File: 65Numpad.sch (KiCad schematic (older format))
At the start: 137 parts

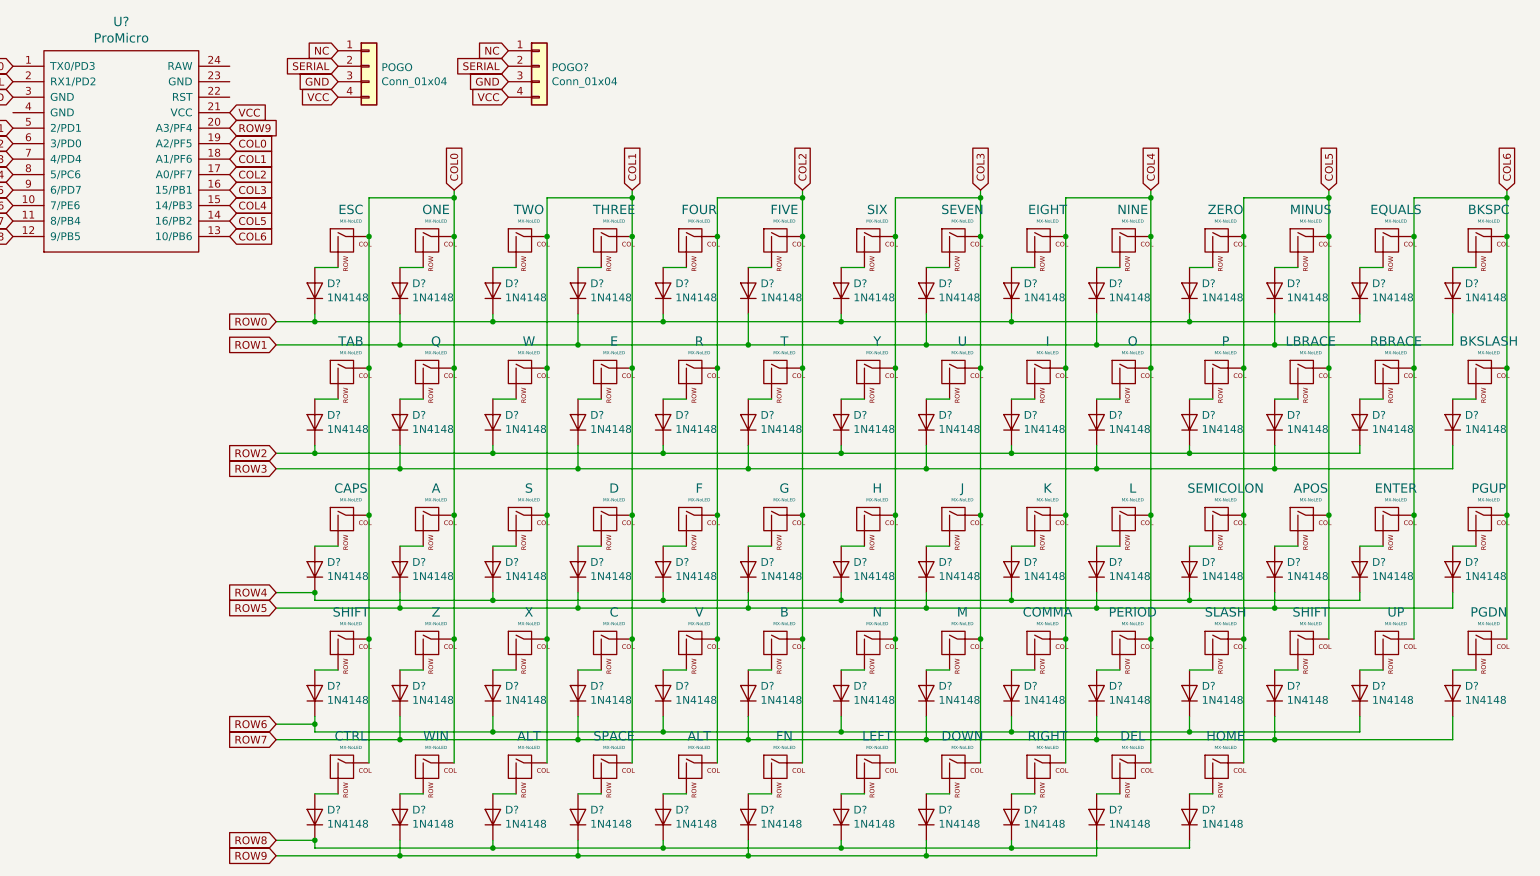
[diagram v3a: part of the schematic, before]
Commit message: Finished assigning footprints
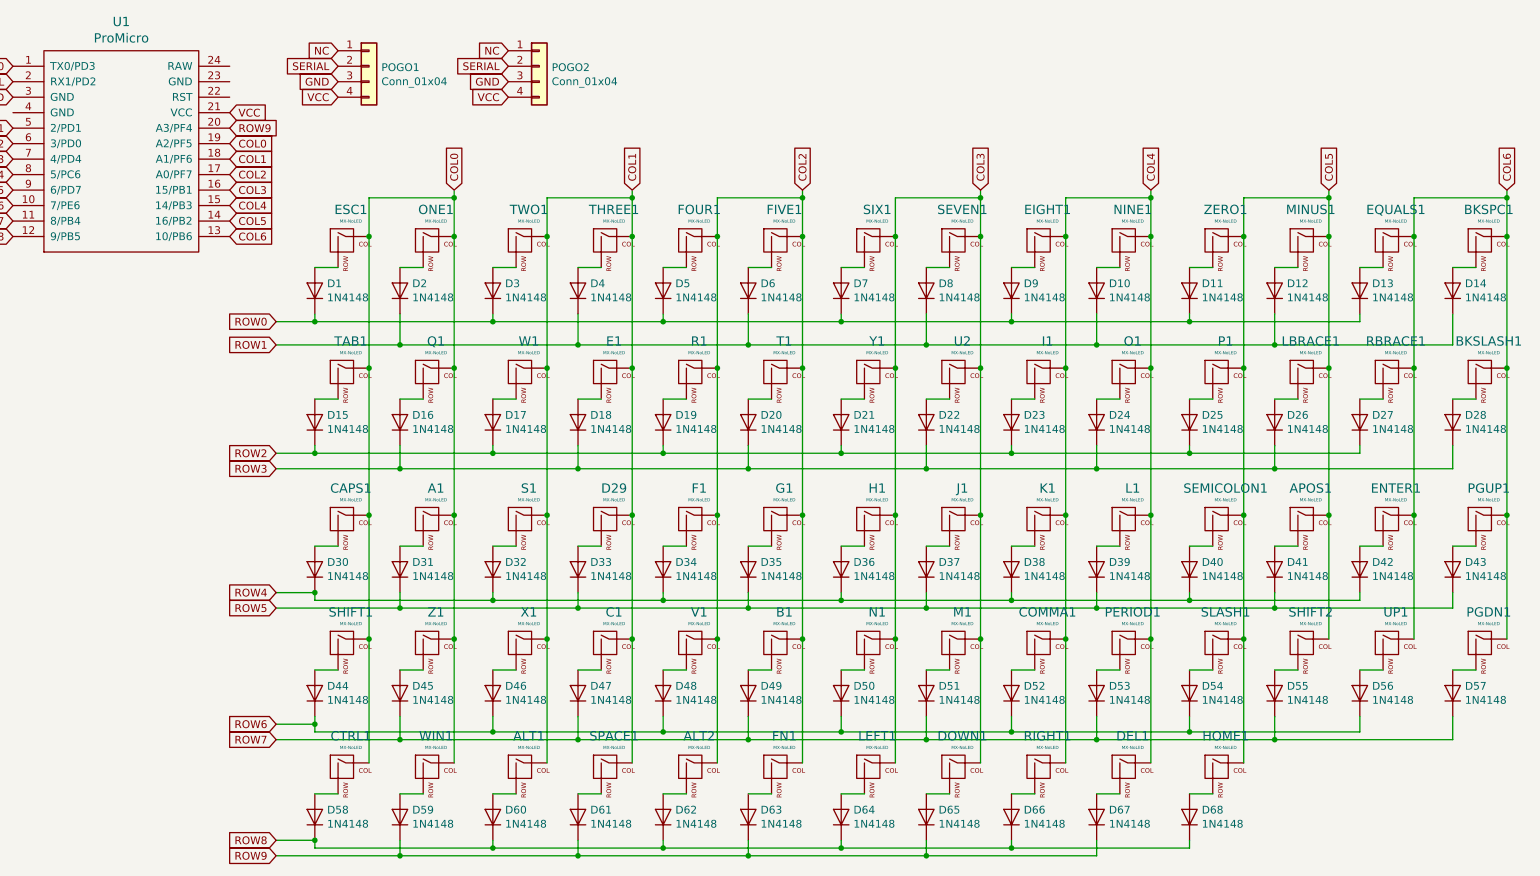
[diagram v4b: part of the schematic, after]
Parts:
- A1: renamed from A; footprint (none) -> MX_Only:MXOnly-1U-NoLED
- ALT1, ALT2: renamed from ALT; footprint (none) -> MX_Only:MXOnly-1.25U-NoLED
- APOS1: renamed from APOS; footprint (none) -> MX_Only:MXOnly-1U-NoLED
- B1: renamed from B; footprint (none) -> MX_Only:MXOnly-1U-NoLED
- BKSLASH1: renamed from BKSLASH; footprint (none) -> MX_Only:MXOnly-1.5U-NoLED
- BKSPC1: renamed from BKSPC; footprint (none) -> MX_Only:MXOnly-2U-NoLED
- C1: renamed from C; footprint (none) -> MX_Only:MXOnly-1U-NoLED
- CAPS1: renamed from CAPS; footprint (none) -> MX_Only:MXOnly-1.75U-NoLED
- COMMA1: renamed from COMMA; footprint (none) -> MX_Only:MXOnly-1U-NoLED
- CTRL1: renamed from CTRL; footprint (none) -> MX_Only:MXOnly-1.25U-NoLED
- D29: renamed from D; footprint (none) -> MX_Only:MXOnly-1U-NoLED
- DEL1: renamed from DEL; footprint (none) -> MX_Only:MXOnly-1U-NoLED
- DOWN1: renamed from DOWN; footprint (none) -> MX_Only:MXOnly-1U-NoLED
- E1: renamed from E; footprint (none) -> MX_Only:MXOnly-1U-NoLED
- EIGHT1: renamed from EIGHT; footprint (none) -> MX_Only:MXOnly-1U-NoLED
- ENTER1: renamed from ENTER; footprint (none) -> MX_Only:MXOnly-2.25U-NoLED
- EQUALS1: renamed from EQUALS; footprint (none) -> MX_Only:MXOnly-1U-NoLED
- ESC1: renamed from ESC; footprint (none) -> MX_Only:MXOnly-1U-NoLED
- F1: renamed from F; footprint (none) -> MX_Only:MXOnly-1U-NoLED
- FIVE1: renamed from FIVE; footprint (none) -> MX_Only:MXOnly-1U-NoLED
- FN1: renamed from FN; footprint (none) -> MX_Only:MXOnly-1.25U-NoLED
- FOUR1: renamed from FOUR; footprint (none) -> MX_Only:MXOnly-1U-NoLED
- G1: renamed from G; footprint (none) -> MX_Only:MXOnly-1U-NoLED
- H1: renamed from H; footprint (none) -> MX_Only:MXOnly-1U-NoLED
- HOME1: renamed from HOME; footprint (none) -> MX_Only:MXOnly-1U-NoLED
- I1: renamed from I; footprint (none) -> MX_Only:MXOnly-1U-NoLED
- J1: renamed from J; footprint (none) -> MX_Only:MXOnly-1U-NoLED
- K1: renamed from K; footprint (none) -> MX_Only:MXOnly-1U-NoLED
- L1: renamed from L; footprint (none) -> MX_Only:MXOnly-1U-NoLED
- LBRACE1: renamed from LBRACE; footprint (none) -> MX_Only:MXOnly-1U-NoLED
- LEFT1: renamed from LEFT; footprint (none) -> MX_Only:MXOnly-1U-NoLED
- M1: renamed from M; footprint (none) -> MX_Only:MXOnly-1U-NoLED
- MINUS1: renamed from MINUS; footprint (none) -> MX_Only:MXOnly-1U-NoLED
- N1: renamed from N; footprint (none) -> MX_Only:MXOnly-1U-NoLED
- NINE1: renamed from NINE; footprint (none) -> MX_Only:MXOnly-1U-NoLED
- O1: renamed from O; footprint (none) -> MX_Only:MXOnly-1U-NoLED
- ONE1: renamed from ONE; footprint (none) -> MX_Only:MXOnly-1U-NoLED
- P1: renamed from P; footprint (none) -> MX_Only:MXOnly-1U-NoLED
- PERIOD1: renamed from PERIOD; footprint (none) -> MX_Only:MXOnly-1U-NoLED
- PGDN1: renamed from PGDN; footprint (none) -> MX_Only:MXOnly-1U-NoLED
- PGUP1: renamed from PGUP; footprint (none) -> MX_Only:MXOnly-1U-NoLED
- POGO1: renamed from POGO; footprint (none) -> Pin_Headers:Pin_Header_Angled_1x04_Pitch2.54mm
- POGO2: renamed from POGO?; footprint (none) -> Pin_Headers:Pin_Header_Angled_1x04_Pitch2.54mm
- Q1: renamed from Q; footprint (none) -> MX_Only:MXOnly-1U-NoLED
- R1: renamed from R; footprint (none) -> MX_Only:MXOnly-1U-NoLED
- RBRACE1: renamed from RBRACE; footprint (none) -> MX_Only:MXOnly-1U-NoLED
- RIGHT1: renamed from RIGHT; footprint (none) -> MX_Only:MXOnly-1U-NoLED
- S1: renamed from S; footprint (none) -> MX_Only:MXOnly-1U-NoLED
- SEMICOLON1: renamed from SEMICOLON; footprint (none) -> MX_Only:MXOnly-1U-NoLED
- SEVEN1: renamed from SEVEN; footprint (none) -> MX_Only:MXOnly-1U-NoLED
- SHIFT1: renamed from SHIFT; footprint (none) -> MX_Only:MXOnly-2.25U-NoLED
- SHIFT2: renamed from SHIFT; footprint (none) -> MX_Only:MXOnly-1.75U-NoLED
- SIX1: renamed from SIX; footprint (none) -> MX_Only:MXOnly-1U-NoLED
- SLASH1: renamed from SLASH; footprint (none) -> MX_Only:MXOnly-1U-NoLED
- SPACE1: renamed from SPACE; footprint (none) -> MX_Only:MXOnly-6.25U-NoLED
- T1: renamed from T; footprint (none) -> MX_Only:MXOnly-1U-NoLED
- TAB1: renamed from TAB; footprint (none) -> MX_Only:MXOnly-1.5U-NoLED
- THREE1: renamed from THREE; footprint (none) -> MX_Only:MXOnly-1U-NoLED
- TWO1: renamed from TWO; footprint (none) -> MX_Only:MXOnly-1U-NoLED
- U1: renamed from U?; footprint (none) -> Keebio-Parts:ArduinoProMicro
- U2: renamed from U; footprint (none) -> MX_Only:MXOnly-1U-NoLED
- UP1: renamed from UP; footprint (none) -> MX_Only:MXOnly-1U-NoLED
- V1: renamed from V; footprint (none) -> MX_Only:MXOnly-1U-NoLED
- W1: renamed from W; footprint (none) -> MX_Only:MXOnly-1U-NoLED
- WIN1: renamed from WIN; footprint (none) -> MX_Only:MXOnly-1.25U-NoLED
- X1: renamed from X; footprint (none) -> MX_Only:MXOnly-1U-NoLED
- Y1: renamed from Y; footprint (none) -> MX_Only:MXOnly-1U-NoLED
- Z1: renamed from Z; footprint (none) -> MX_Only:MXOnly-1U-NoLED
- ZERO1: renamed from ZERO; footprint (none) -> MX_Only:MXOnly-1U-NoLED
- gave numbers to parts that had none: 67

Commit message: Arranged PCB
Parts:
- added U3: MCP23017_SP, Package_DIP:DIP-28_W7.62mm, symbol Interface_Expansion:MCP23017_SP
- A1, APOS1, B1, C1, COMMA1, D29, DEL1, DOWN1, E1, EIGHT1, EQUALS1, ESC1, F1, FIVE1, FOUR1, G1, H1, HOME1, I1, J1, K1, L1, LBRACE1, LEFT1, M1, MINUS1, N1, NINE1, O1, ONE1, P1, PERIOD1, PGDN1, PGUP1, Q1, R1, RBRACE1, RIGHT1, S1, SEMICOLON1, SEVEN1, SIX1, SLASH1, T1, THREE1, TWO1, U2, UP1, V1, W1, X1, Y1, Z1, ZERO1: footprint MX_Only:MXOnly-1U-NoLED -> MX_Only:MXOnly-1U-NoLEDHotswap
- ALT1, ALT2, CTRL1, FN1, WIN1: footprint MX_Only:MXOnly-1.25U-NoLED -> MX_Only:MXOnly-1.25U-NoLEDHotswap
- BKSLASH1, TAB1: footprint MX_Only:MXOnly-1.5U-NoLED -> MX_Only:MXOnly-1.5U-NoLEDHotswap
- BKSPC1: footprint MX_Only:MXOnly-2U-NoLED -> MX_Only:MXOnly-2U-NoLEDHotswap
- CAPS1, SHIFT2: footprint MX_Only:MXOnly-1.75U-NoLED -> MX_Only:MXOnly-1.75U-NoLEDHotswap
- D1, D10, D11, D12, D13, D14, D15, D16, D17, D18, D19, D2, D20, D21, D22, D23, D24, D25, D26, D27, D28, D3, D30, D31, D32, D33, D34, D35, D36, D37, D38, D39, D4, D40, D41, D42, D43, D44, D45, D46, D47, D48, D49, D5, D50, D51, D52, D53, D54, D55, D56, D57, D58, D59, D6, D60, D61, D62, D63, D64, D65, D66, D67, D68, D7, D8, D9: footprint Diode_THT:D_DO-35_SOD27_P7.62mm_Horizontal -> Diodes_THT:D_DO-35_SOD27_P7.62mm_Horizontal
- ENTER1, SHIFT1: footprint MX_Only:MXOnly-2.25U-NoLED -> MX_Only:MXOnly-2.25U-NoLEDHotswap
- SPACE1: footprint MX_Only:MXOnly-6.25U-NoLED -> MX_Only:MXOnly-6.25U-NoLEDHotswap
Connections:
- net COL0: now also U3.22 (GPA1); no longer U1.19 (A2/PF5)
- net COL1: now also U3.23 (GPA2); no longer U1.18 (A1/PF6)
- net COL2: now also U3.24 (GPA3); no longer U1.17 (A0/PF7)
- net COL3: now also U3.25 (GPA4); no longer U1.16 (15/PB1)
- net COL4: now also PGUP1.1 (COL), U3.26 (GPA5); no longer DEL1.1 (COL), U1.15 (14/PB3)
- net COL5: now also PGDN1.1 (COL), U3.27 (GPA6); no longer HOME1.1 (COL), U1.14 (16/PB2)
- net COL6: now also DEL1.1 (COL), HOME1.1 (COL), U3.28 (GPA7); no longer PGDN1.1 (COL), PGUP1.1 (COL), U1.13 (10/PB6)
- net GND: now also U1.23 (GND), U3.10 (VSS), U3.15 (A0), U3.16 (A1), U3.17 (A2)
- net ROW0: now also U1.7 (4/PD4); no longer U1.1 (TX0/PD3)
- net ROW1: now also U3.1 (GPB0); no longer U1.5 (2/PD1)
- net ROW2: now also U3.2 (GPB1); no longer U1.6 (3/PD0)
- net ROW3: now also U3.3 (GPB2); no longer U1.7 (4/PD4)
- net ROW4: now also U3.4 (GPB3); no longer U1.8 (5/PC6)
- net ROW5: now also U3.5 (GPB4); no longer U1.9 (6/PD7)
- net ROW6: now also U3.6 (GPB5); no longer U1.10 (7/PE6)
- net ROW7: now also U3.7 (GPB6); no longer U1.11 (8/PB4)
- net ROW8: now also D59.1 (K), D61.1 (K), D63.1 (K), D65.1 (K), D67.1 (K), U3.21 (GPA0), U3.8 (GPB7); no longer U1.12 (9/PB5)
- net VCC: now also U3.9 (VDD)
- net at DEL1.2 (ROW): now also D43.2 (A); no longer D67.2 (A)
- net at HOME1.2 (ROW): now also D57.2 (A); no longer D68.2 (A)
- net at PGUP1.2 (ROW): now also D67.2 (A); no longer D43.2 (A)
- net at PGDN1.2 (ROW): now also D68.2 (A); no longer D57.2 (A)
- net NC: no longer names the net of POGO2.1 (Pin_1)
- net NC: no longer POGO1.1 (Pin_1)
- removed net ROW9: D59.1 (K), D61.1 (K), D63.1 (K), D65.1 (K), D67.1 (K), U1.20 (A3/PF4)
- new net SCL: U1.6 (3/PD0), U3.12 (SCK)
- new net SDA: U1.5 (2/PD1), U3.13 (SDA)
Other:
- moved on the sheet: A1, ALT1, ALT2, APOS1, B1, BKSLASH1, BKSPC1, C1, CAPS1, COMMA1, CTRL1, D1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

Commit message: Almost done routing
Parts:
- removed U3: MCP23017_SP, Package_DIP:DIP-28_W7.62mm, symbol Interface_Expansion:MCP23017_SP
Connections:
- net SCL is gone; now on net COL2: U1.6 (3/PD0)
- net SDA is gone; now on net ROW7: U1.5 (2/PD1)
- net COL0: now also U1.20 (A3/PF4)
- net COL1: now also U1.15 (14/PB3)
- net COL3: now also U1.7 (4/PD4)
- net COL4: now also U1.10 (7/PE6)
- net COL5: now also U1.11 (8/PB4)
- net COL6: now also U1.12 (9/PB5)
- net ROW0: now also U1.19 (A2/PF5); no longer U1.7 (4/PD4)
- net ROW1: now also U1.18 (A1/PF6)
- net ROW2: now also U1.17 (A0/PF7)
- net ROW3: now also U1.16 (15/PB1)
- net ROW4: now also U1.14 (16/PB2)
- net ROW5: now also U1.13 (10/PB6)
- net ROW6: now also U1.1 (TX0/PD3)
- net ROW8: now also U1.8 (5/PC6); no longer D59.1 (K), D61.1 (K), D63.1 (K), D65.1 (K), D67.1 (K)
- net ROW9: now reaches U1.9 (6/PD7)
- net ROW9: now also D59.1 (K), D61.1 (K), D63.1 (K), D65.1 (K), D67.1 (K)
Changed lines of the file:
@@
 Connection ~ 3350 6000
-Wire Wire Line
-	6150 6050 6750 6050
 Wire Wire Line
 	3900 6000 3900 6100
@@
 	5600 6000 5600 6050
 Connection ~ 5600 6050
-Wire Wire Line
-	5600 6050 6150 6050
 Connection ~ 6150 6100
 Wire Wire Line
@@
 Text GLabel 4050 1100 0    50   Input ~ 0
 GND
-$Comp
-L Interface_Expansion:MCP23017_SP U3
-U 1 1 602098ED
-P 1550 4150
-F 0 "U3" H 1550 5431 50  0000 C CNN
-F 1 "MCP23017_SP" H 1550 5340 50  0000 C CNN
-F 2 "Package_DIP:DIP-28_W7.62mm" H 1750 3150 50  0001 L CNN
-F 3 "http://ww1.microchip.com/downloads/en/DeviceDoc/20001952C.pdf" H 1750 3050 50  0001 L CNN
-	1    1550 4150
-	1    0    0    -1
-$EndComp
-Connection ~ 6150 6050
 Wire Wire Line
 	6150 6050 6150 6100
-Text GLabel 1550 5250 3    50   Input ~ 0
-GND
-Text GLabel 1550 3050 1    50   Input ~ 0
-VCC
-Text GLabel 700  4850 0    50   Input ~ 0
-GND
 Text GLabel 2250 1100 2    50   Input ~ 0
 GND
+Text GLabel 2250 1400 2    50   Input ~ 0
+COL0
+Text GLabel 2250 1600 2    50   Input ~ 0
+ROW1
+Text GLabel 2250 1500 2    50   Input ~ 0
+ROW0
+Text GLabel 2250 1700 2    50   Input ~ 0
+ROW2
+Text GLabel 2250 1800 2    50   Input ~ 0
+ROW3
+Text GLabel 2250 1900 2    50   Input ~ 0
+COL1
+Text GLabel 2250 2100 2    50   Input ~ 0
+ROW5
+Text GLabel 2250 2000 2    50   Input ~ 0
+ROW4
+Text GLabel 850  1500 0    50   Input ~ 0
+COL2
+Text GLabel 850  1000 0    50   Input ~ 0
+ROW6
 Text GLabel 850  1400 0    50   Input ~ 0
-SDA
-Text GLabel 850  1500 0    50   Input ~ 0
-SCL
-Text GLabel 850  3350 0    50   Input ~ 0
-SDA
-Text GLabel 850  3450 0    50   Input ~ 0
-SCL
+ROW7
+Text GLabel 850  1600 0    50   Input ~ 0
+COL3
 Wire Wire Line
-	850  4950 800  4950
-Wire Wire Line
-	800  4950 800  4850
-Wire Wire Line
-	800  4850 700  4850
-Wire Wire Line
-	800  4850 850  4850
-Connection ~ 800  4850
-Wire Wire Line
-	800  4850 800  4750
-Wire Wire Line
-	800  4750 850  4750
-Text GLabel 2250 4950 2    50   Input ~ 0
+	5600 6050 6750 6050
+Text GLabel 850  1700 0    50   Input ~ 0
+ROW8
+Text GLabel 850  1800 0    50   Input ~ 0
+ROW9
+Text GLabel 850  1900 0    50   Input ~ 0
+COL4
+Text GLabel 850  2000 0    50   Input ~ 0
+COL5
+Text GLabel 850  2100 0    50   Input ~ 0
 COL6
-Text GLabel 2250 4850 2    50   Input ~ 0
-COL5
-Text GLabel 2250 4750 2    50   Input ~ 0
-COL4
-Text GLabel 2250 4650 2    50   Input ~ 0
-COL3
-Text GLabel 2250 4550 2    50   Input ~ 0
-COL2
-Text GLabel 2250 4450 2    50   Input ~ 0
-COL1
-Text GLabel 2250 4350 2    50   Input ~ 0
-COL0
-Text GLabel 2250 4250 2    50   Input ~ 0
-ROW9
-Text GLabel 2250 4050 2    50   Input ~ 0
-ROW8
-Text GLabel 2250 3950 2    50   Input ~ 0
-ROW7
-Text GLabel 2250 3850 2    50   Input ~ 0
-ROW6
-Text GLabel 2250 3750 2    50   Input ~ 0
-ROW5
-Text GLabel 2250 3550 2    50   Input ~ 0
-ROW3
-Text GLabel 2250 3650 2    50   Input ~ 0
-ROW4
-Text GLabel 2250 3450 2    50   Input ~ 0
-ROW2
-Text GLabel 2250 3350 2    50   Input ~ 0
-ROW1
-Text GLabel 850  1600 0    50   Input ~ 0
-ROW0
 $EndSCHEMATC

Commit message: Routed numpad
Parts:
- added ASTERISK1, DEL2, EIGHT2, FIVE2, FOUR2, MINUS2, NINE2, NUM1, ONE2, SEVEN2, SIX2, SLASH2, THREE2, TWO2: MX-NoLED, MX_Only:MXOnly-1U-NoLEDHotswap, symbol MX_Alps_Hybrid:MX-NoLED
- added D69, D70, D71, D72, D73, D74, D75, D76, D77, D78, D79, D80, D81, D82, D83, D84, D85: 1N4148, Diodes_THT:D_DO-35_SOD27_P7.62mm_Horizontal, symbol Diode:1N4148
- added ENTER2, PLUS1, ZERO2: MX-NoLED, MX_Only:MXOnly-2U-NoLEDHotswap, symbol MX_Alps_Hybrid:MX-NoLED
- added Numpad1: ProMicro, Keebio-Parts:ArduinoProMicro, symbol keebio:ProMicro
- added POGO3, POGO4: Conn_01x04, Pin_Headers:Pin_Header_Angled_1x04_Pitch2.54mm, symbol Connector_Generic:Conn_01x04
- renumbered U1 to Main1
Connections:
- net COL0: now also FOUR2.1 (COL), NUM1.1 (COL), Numpad1.5 (2/PD1), ONE2.1 (COL), SEVEN2.1 (COL), ZERO2.1 (COL)
- net COL1: now also EIGHT2.1 (COL), FIVE2.1 (COL), Numpad1.20 (A3/PF4), SLASH2.1 (COL), TWO2.1 (COL)
- net COL2: now also ASTERISK1.1 (COL), DEL2.1 (COL), NINE2.1 (COL), Numpad1.19 (A2/PF5), SIX2.1 (COL), THREE2.1 (COL)
- net COL3: now also ENTER2.1 (COL), MINUS2.1 (COL), Numpad1.18 (A1/PF6), PLUS1.1 (COL)
- net GND: now also Main1.4 (GND), Numpad1.23 (GND), Numpad1.3 (GND), Numpad1.4 (GND), POGO3.3 (Pin_3), POGO4.3 (Pin_3)
- net ROW0: now also D69.1 (K), D70.1 (K), D71.1 (K), D72.1 (K), Numpad1.6 (3/PD0)
- net ROW1: now also D73.1 (K), D74.1 (K), D75.1 (K), Numpad1.7 (4/PD4)
- net ROW2: now also D76.1 (K), D77.1 (K), D78.1 (K), D79.1 (K), Numpad1.8 (5/PC6)
- net ROW3: now also D80.1 (K), D81.1 (K), D82.1 (K), Numpad1.9 (6/PD7)
- net ROW4: now also D83.1 (K), D84.1 (K), D85.1 (K), Numpad1.10 (7/PE6)
- net SERIAL: now also POGO1.1 (Pin_1), POGO2.1 (Pin_1), Numpad1.2 (RX1/PD2), POGO3.1 (Pin_1), POGO4.1 (Pin_1); no longer POGO1.2 (Pin_2), POGO2.2 (Pin_2)
- net VCC: now also Numpad1.21 (VCC), POGO3.4 (Pin_4), POGO4.4 (Pin_4)
- new net: D69.2 (A), NUM1.2 (ROW)
- new net: D73.2 (A), SEVEN2.2 (ROW)
- new net: D76.2 (A), FOUR2.2 (ROW)
- new net: D80.2 (A), ONE2.2 (ROW)
- new net: D83.2 (A), ZERO2.2 (ROW)
- new net: D70.2 (A), SLASH2.2 (ROW)
- new net: D74.2 (A), EIGHT2.2 (ROW)
- new net: D77.2 (A), FIVE2.2 (ROW)
- new net: D81.2 (A), TWO2.2 (ROW)
- new net: ASTERISK1.2 (ROW), D71.2 (A)
- new net: D75.2 (A), NINE2.2 (ROW)
- new net: D78.2 (A), SIX2.2 (ROW)
- new net: D82.2 (A), THREE2.2 (ROW)
- new net: D84.2 (A), DEL2.2 (ROW)
- new net: D72.2 (A), MINUS2.2 (ROW)
- new net: D79.2 (A), PLUS1.2 (ROW)
- new net: D85.2 (A), ENTER2.2 (ROW)
